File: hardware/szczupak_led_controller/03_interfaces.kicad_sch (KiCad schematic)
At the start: 0 parts

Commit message: #3 Added some libraries for basic components in interfaces schematic
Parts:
- added J2: USB4110-GF-A, szczupak_led_controller:USB4110GFA, symbol szczupak_led_controller:USB4110-GF-A
- added R6: 5k1, Resistor_SMD:R_0603_1608Metric, symbol Device:R
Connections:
- new net: J2.A5, R6.2
- new net GND: R6.1
- new net VBUS: J2.A4, J2.A9, J2.B4, J2.B9
- no-connect marks 0 -> 4

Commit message: Repository cleanup and merge of two versions of interface_schematic
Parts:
- removed J2: USB4110-GF-A, szczupak_led_controller:USB4110GFA, symbol szczupak_led_controller:USB4110-GF-A
- added IC2: SN65HVD230DR, SOT127P600X175-8N, symbol SN65HVD230DR:SN65HVD230DR
- added J2: USB4085-GF-A_REVA4, USB4085-GF-A_REVA4:GCT_USB4085-GF-A_REVA4, symbol USB4085-GF-A_REVA4:USB4085-GF-A_REVA4
- added J3: (no value), symbol XY2500V-D(5.08)-4PIN:XY2500V-D(5.08)-4PIN
- added R7: 5.1k, symbol Device:R
- added R8: 120, symbol Device:R
- added S3: PESD1CAN_215, PESD1CAN_215:DIO_PESD1CAN_215, symbol PESD1CAN_215:PESD1CAN_215
- added U1: USBLC6-2SC6, Package_TO_SOT_SMD:SOT-23-6, symbol Power_Protection:USBLC6-2SC6
- added U2: RCD-24, Converter_DCDC:Converter_DCDC_RECOM_RCD-24_THT, symbol Driver_LED:RCD-24
- R6: value 5k1 -> 5.1k; footprint Resistor_SMD:R_0603_1608Metric -> (none)
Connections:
- net GND: now also R6.2, IC2.2 (GND), IC2.8 (RS), J2.A1 (GND), J2.A12 (GND), J2.B1 (GND), J2.B12 (GND), J2.S1 (SHELL), J2.S2 (SHELL), J2.S3 (SHELL), J2.S4 (SHELL), J3.2, R7.2, S3.3, U1.2 (GND), U2.4 (GND); no longer R6.1
- net VBUS: now also J2.A4 (VBUS), J2.A9 (VBUS), J2.B4 (VBUS), J2.B9 (VBUS)
- new net: J2.A5 (CC1), R7.1
- new net: J2.A7 (DN1), J2.B7 (DN2), U1.1 (I/O1)
- new net: J2.A6 (DP1), J2.B6 (DP2), U1.3 (I/O2)
- new net: J2.B5 (CC2), R6.1
- new net +12V: J3.1, U2.1 (+Vin)
- new net +3.3V: IC2.3 (VCC)
- new net CANH: IC2.7 (CANH), J3.3, R8.1, S3.1
- new net CANL: IC2.6 (CANL), J3.4, R8.2, S3.2
- new net CAN_RX: IC2.4 (R)
- new net CAN_TX: IC2.1 (D)
- new net DIM_LED1: U2.2 (Analogue_Dimming)
- new net LED1+: U2.6 (+Vout)
- new net LED1-: U2.5 (-Vout)
- new net PWM_LED1: U2.3 (PWM/ON/OFF)
- new net USB_5V: U1.5 (VBUS)
- new net USB_DM: U1.6 (I/O1)
- new net USB_DP: U1.4 (I/O2)
- no-connect marks 4 -> 3

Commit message: #5 #3 Added first version of power_input schematic with some required libraries
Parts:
- R6, R7: footprint (none) -> Resistor_SMD:R_0603_1608Metric
- R8: footprint (none) -> Resistor_SMD:R_0805_2012Metric
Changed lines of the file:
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@@
 			)
 		)
-		(property "Footprint" ""
+		(property "Footprint" "Resistor_SMD:R_0603_1608Metric"
 			(at 157.988 33.02 90)
 			(hide yes)
@@
 			)
 		)
-		(property "Footprint" ""
+		(property "Footprint" "Resistor_SMD:R_0805_2012Metric"
 			(at 27.432 95.25 90)
 			(hide yes)
@@
 			)
 		)
-		(property "Footprint" ""
+		(property "Footprint" "Resistor_SMD:R_0603_1608Metric"
 			(at 149.098 33.02 90)
 			(hide yes)
@@
 		)
 	)
-	(embedded_fonts no)
 )

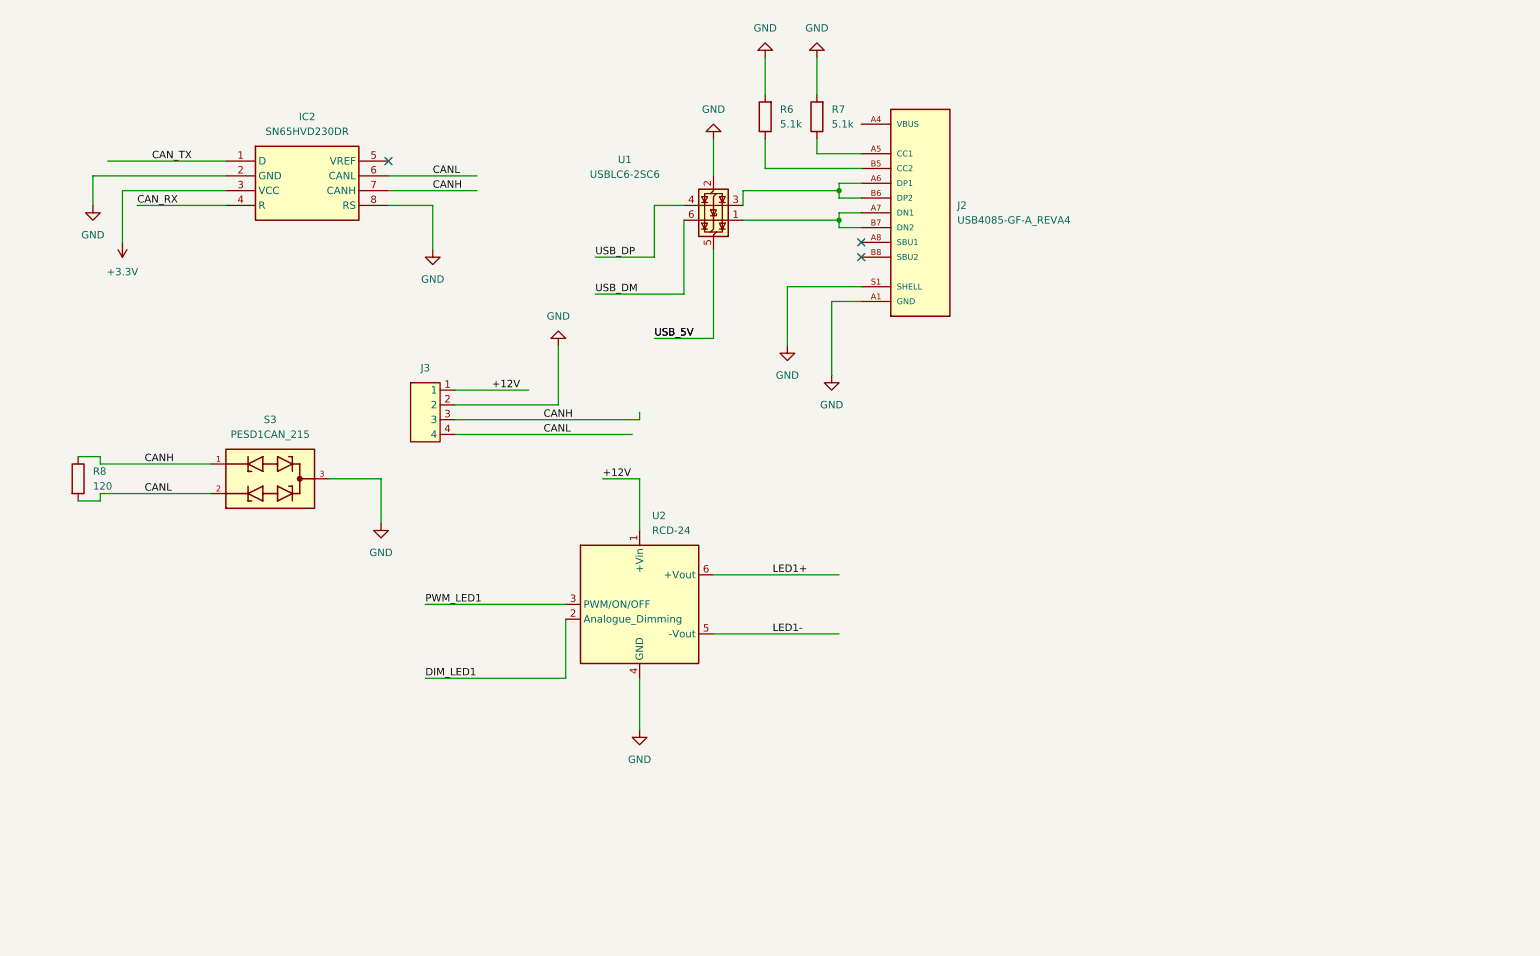
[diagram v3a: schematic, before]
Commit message: #4 #6 Added power output and interfaces schematics
Designed initial placement for most important components on pcb
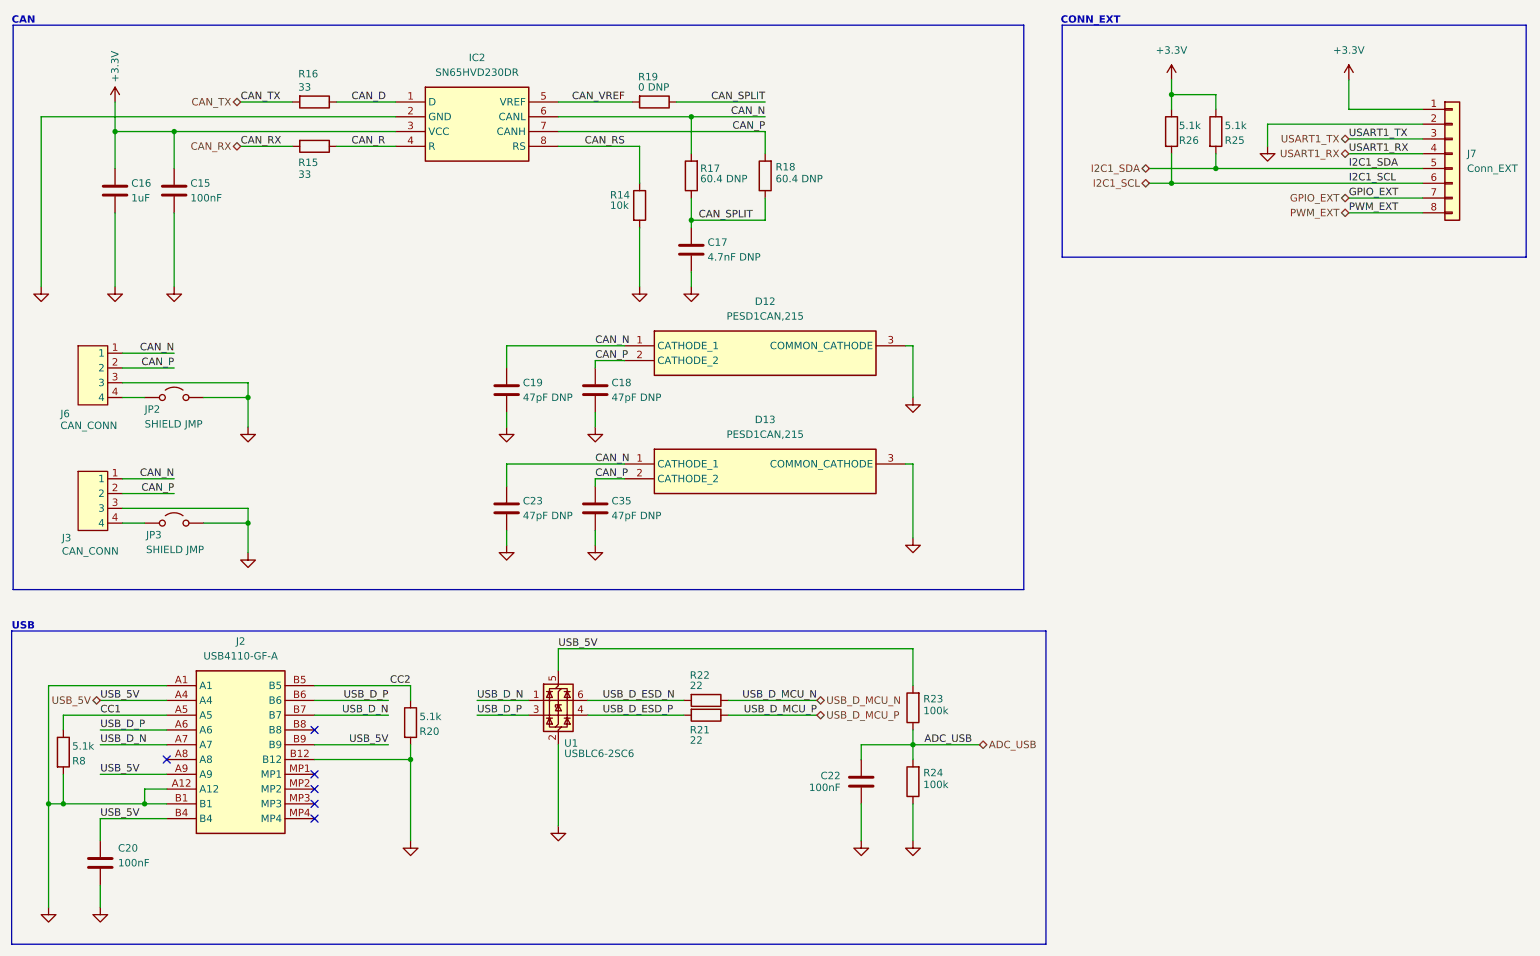
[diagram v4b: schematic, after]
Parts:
- removed J2: USB4085-GF-A_REVA4, USB4085-GF-A_REVA4:GCT_USB4085-GF-A_REVA4, symbol USB4085-GF-A_REVA4:USB4085-GF-A_REVA4
- removed R6, R7: 5.1k, Resistor_SMD:R_0603_1608Metric, symbol Device:R
- removed S3: PESD1CAN_215, PESD1CAN_215:DIO_PESD1CAN_215, symbol PESD1CAN_215:PESD1CAN_215
- removed U2: RCD-24, Converter_DCDC:Converter_DCDC_RECOM_RCD-24_THT, symbol Driver_LED:RCD-24
- added C15, C20, C22: 100nF, Capacitor_SMD:C_0603_1608Metric, symbol Device:C
- added C16: 1uF, Capacitor_SMD:C_0805_2012Metric, symbol Device:C
- added C17: 4.7nF DNP, Capacitor_SMD:C_0603_1608Metric, symbol Device:C
- added C18, C19, C23, C35: 47pF DNP, Capacitor_SMD:C_0603_1608Metric, symbol Device:C
- added D12, D13: PESD1CAN,215, szczupak_led_controller:SOT95P230X110-3N, symbol szczupak_led_controller:PESD1CAN,215
- added J2: USB4110-GF-A, szczupak_led_controller:USB4110GFA, symbol szczupak_led_controller:USB4110-GF-A
- added J6: CAN_CONN, szczupak_led_controller:XY2500V-D(5.08)-4PIN, symbol XY2500V-D(5.08)-4PIN:XY2500V-D(5.08)-4PIN
- added J7: Conn_EXT, Connector_PinHeader_2.54mm:PinHeader_1x08_P2.54mm_Vertical, symbol Connector_Generic:Conn_01x08
- added JP2, JP3: SHIELD JMP, Jumper:SolderJumper-2_P1.3mm_Open_TrianglePad1.0x1.5mm, symbol Jumper:Jumper_2_Open
- added R14: 10k, Resistor_SMD:R_0603_1608Metric, symbol Device:R
- added R15, R16: 33, Resistor_SMD:R_0603_1608Metric, symbol Device:R
- added R17, R18: 60.4 DNP, Resistor_SMD:R_0805_2012Metric, symbol Device:R
- added R19: 0 DNP, Resistor_SMD:R_0603_1608Metric, symbol Device:R
- added R20, R25, R26: 5.1k, Resistor_SMD:R_0603_1608Metric, symbol Device:R
- added R21, R22: 22, Resistor_SMD:R_0603_1608Metric, symbol Device:R
- added R23, R24: 100k, Resistor_SMD:R_0603_1608Metric, symbol Device:R
- IC2: footprint SOT127P600X175-8N -> szczupak_led_controller:SOT127P600X175-8N
- J3: value (none) -> CAN_CONN; footprint (none) -> szczupak_led_controller:XY2500V-D(5.08)-4PIN
- R8: value 120 -> 5.1k; footprint Resistor_SMD:R_0805_2012Metric -> Resistor_SMD:R_0603_1608Metric
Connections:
- net +3.3V: now also C15.1, C16.1, J7.1 (Pin_1), R25.1, R26.1
- net CAN_RX: now also R15.2; no longer IC2.4 (R)
- net CAN_TX: now also R16.2; no longer IC2.1 (D)
- net GND: now also J3.3, R8.2, C15.2, C16.2, C17.2, C18.2, C19.2, C20.2, C22.2, C23.2, C35.2, D12.3 (COMMON_CATHODE), D13.3 (COMMON_CATHODE), J2.A1, J2.A12, J2.B1, J2.B12, J6.3, J7.2 (Pin_2), JP2.2 (B), JP3.2 (B), R14.2, R20.2, R24.1; no longer IC2.8 (RS), J3.2
- net USB_5V: now also C20.1, J2.A4, J2.A9, J2.B4, J2.B9, R23.2
- net CAN_VREF: now reaches IC2.5 (VREF)
- net CAN_VREF: now also R19.2
- net USB_D_N: now reaches U1.1 (I/O1)
- net USB_D_N: now also J2.A7, J2.B7
- net USB_D_P: now reaches U1.3 (I/O2)
- net USB_D_P: now also J2.A6, J2.B6
- net +12V renamed CAN_N
- net CAN_N: now also IC2.6 (CANL), C19.1, C23.1, D12.1 (CATHODE_1), D13.1 (CATHODE_1), J6.1, R17.2
- removed net CANH: IC2.7 (CANH), J3.3, R8.1
- removed net CANL: IC2.6 (CANL), J3.4, R8.2
- net USB_DM renamed USB_D_ESD_N
- net USB_D_ESD_N: now also R22.2
- net USB_DP renamed USB_D_ESD_P
- net USB_D_ESD_P: now also R21.2
- new net: J3.4, JP3.1 (A)
- new net: J6.4, JP2.1 (A)
- new net ADC_USB: C22.1, R23.1, R24.2
- new net CAN_D: IC2.1 (D), R16.1
- new net CAN_P: C18.1, C35.1, D12.2 (CATHODE_2), D13.2 (CATHODE_2), IC2.7 (CANH), J3.2, J6.2, R18.2
- new net CAN_R: IC2.4 (R), R15.1
- new net CAN_RS: IC2.8 (RS), R14.1
- new net CAN_SPLIT: C17.1, R17.1, R18.1, R19.1
- new net CC1: J2.A5, R8.1
- new net CC2: J2.B5, R20.1
- new net GPIO_EXT: J7.7 (Pin_7)
- new net I2C1_SCL: J7.6 (Pin_6), R26.2
- new net I2C1_SDA: J7.5 (Pin_5), R25.2
- new net PWM_EXT: J7.8 (Pin_8)
- new net USART1_RX: J7.4 (Pin_4)
- new net USART1_TX: J7.3 (Pin_3)
- new net USB_D_MCU_N: R22.1
- new net USB_D_MCU_P: R21.1
- no-connect marks 3 -> 6
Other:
- note added: "CAN"
- note added: "CONN_EXT"
- note added: "USB"
- company: (none) -> AGH Marines
- title: (none) -> szczupak_led_controller - 03_interfaces
- moved on the sheet: IC2, J3, U1

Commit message: #8 Finished initial component placement on pcb
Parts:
- removed C23, C35: 47pF DNP, Capacitor_SMD:C_0603_1608Metric, symbol Device:C
- removed D13: PESD1CAN,215, szczupak_led_controller:SOT95P230X110-3N, symbol szczupak_led_controller:PESD1CAN,215
- removed J7: Conn_EXT, Connector_PinHeader_2.54mm:PinHeader_1x08_P2.54mm_Vertical, symbol Connector_Generic:Conn_01x08
- added J7: Conn_EXT, Connector_PinHeader_2.54mm:PinHeader_1x10_P2.54mm_Vertical, symbol Connector_Generic:Conn_01x10
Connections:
- net +3.3V: now also J7.1 (Pin_1); no longer C15.1, C16.1
- net GND: now also J7.2 (Pin_2); no longer C15.2, C16.2
- net GPIO_EXT: now also J7.9 (Pin_9)
- net I2C1_SCL: now also J7.8 (Pin_8)
- net I2C1_SDA: now also J7.7 (Pin_7)
- net PWM_EXT: now also J7.10 (Pin_10)
- net USART1_RX: now also J7.6 (Pin_6)
- net USART1_TX: now also J7.5 (Pin_5)
- new net NRST: J7.4 (Pin_4)
- new net SWCLK_BOOT0: J7.3 (Pin_3)
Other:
- moved on the sheet: C15, C16, C18, C19, D12, R25, R26

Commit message: #8 Added routing for usb and mcu. Started pouring of power elements
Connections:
- net +3.3V: now also C15.1, C16.1
- net GND: now also C15.2, C16.2
- net GPIO_EXT: now also J7.10 (Pin_10); no longer J7.9 (Pin_9)
- net PWM_EXT: now also J7.9 (Pin_9); no longer J7.10 (Pin_10)
- net CAN_SHIELD_2: now reaches J3.4, JP3.1 (A)
- net CAN_SHIELD_1: now reaches J6.4, JP2.1 (A)
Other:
- moved on the sheet: C15, C16, JP2, JP3
